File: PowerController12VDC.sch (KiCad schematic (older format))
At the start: 1 part

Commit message: Start power supply
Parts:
- added C?: GRM033R71E331KA01D, CAPC0603X33N, symbol GRM033R71E331KA01D:GRM033R71E331KA01D
- added C?: C3216X6S1V106K160AC, CAPC3216X180N, symbol C3216X6S1V106K160AC:C3216X6S1V106K160AC
- added C?: EEE-FK1E330P, CAPAE660X610N, symbol EEE-FK1E330P:EEE-FK1E330P
- added L?: LQM18PNR47NC0L, INDC1608X55N, symbol LQM18PNR47NC0L:LQM18PNR47NC0L
- added R?: ERJ-3RSFR10V, RESC1608X55N, symbol ERJ-3RSFR10V:ERJ-3RSFR10V
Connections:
- net labels added: +12V, GND
- wire segments 0 -> 18
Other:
- moved on the sheet: U?
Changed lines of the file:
@@
 L TPSM84209RKHT:TPSM84209RKHT U?
 U 1 1 5FCF8D29
-P 2700 2100
-F 0 "U?" H 2700 2566 50  0000 C CNN
-F 1 "TPSM84209RKHT" H 2700 2475 50  0000 C CNN
-F 2 "VREG_TPSM84209RKHT" H 2700 2100 50  0001 L BNN
-F 3 "" H 2700 2100 50  0001 L BNN
-F 4 "TPSM84209RKHT" H 2700 2100 50  0001 L BNN "MP"
-F 5 "Unavailable" H 2700 2100 50  0001 L BNN "AVAILABILITY"
-F 6 "Texas Instruments" H 2700 2100 50  0001 L BNN "MF"
-F 7 "4.5V-28V Input, 1.2V-6.0V Output, 2.5-A Power Module 9-QFN-FCMOD -40 to 85" H 2700 2100 50  0001 L BNN "DESCRIPTION"
-F 8 "PowerQFN-9 Texas Instruments" H 2700 2100 50  0001 L BNN "PACKAGE"
-F 9 "Manufacturer Recommendations" H 2700 2100 50  0001 L BNN "STANDARD"
-F 10 "None" H 2700 2100 50  0001 L BNN "PRICE"
-F 11 "C" H 2700 2100 50  0001 L BNN "PARTREV"
-	1    2700 2100
+P 5450 2050
+F 0 "U?" H 5450 2516 50  0000 C CNN
+F 1 "TPSM84209RKHT" H 5450 2425 50  0000 C CNN
+F 2 "VREG_TPSM84209RKHT" H 5450 2050 50  0001 L BNN
+F 3 "" H 5450 2050 50  0001 L BNN
+F 4 "TPSM84209RKHT" H 5450 2050 50  0001 L BNN "MP"
+F 5 "Unavailable" H 5450 2050 50  0001 L BNN "AVAILABILITY"
+F 6 "Texas Instruments" H 5450 2050 50  0001 L BNN "MF"
+F 7 "4.5V-28V Input, 1.2V-6.0V Output, 2.5-A Power Module 9-QFN-FCMOD -40 to 85" H 5450 2050 50  0001 L BNN "DESCRIPTION"
+F 8 "PowerQFN-9 Texas Instruments" H 5450 2050 50  0001 L BNN "PACKAGE"
+F 9 "Manufacturer Recommendations" H 5450 2050 50  0001 L BNN "STANDARD"
+F 10 "None" H 5450 2050 50  0001 L BNN "PRICE"
+F 11 "C" H 5450 2050 50  0001 L BNN "PARTREV"
+	1    5450 2050
 	1    0    0    -1
 $EndComp
+$Comp
+L GRM033R71E331KA01D:GRM033R71E331KA01D C?
+U 1 1 5FCFC38C
+P 5350 2650
+F 0 "C?" H 5400 2890 50  0000 C CNN
+F 1 "GRM033R71E331KA01D" H 5400 2799 50  0000 C CNN
+F 2 "CAPC0603X33N" H 5350 2650 50  0001 L BNN
+F 3 "" H 5350 2650 50  0001 L BNN
+	1    5350 2650
+	1    0    0    -1
+$EndComp
+Wire Wire Line
+	5550 2650 6350 2650
+Wire Wire Line
+	6350 2650 6350 1850
+Wire Wire Line
+	6350 1850 6150 1850
+Wire Wire Line
+	5250 2650 4500 2650
+Wire Wire Line
+	4500 2650 4500 2050
+Wire Wire Line
+	4500 2050 4750 2050
+$Comp
+L LQM18PNR47NC0L:LQM18PNR47NC0L L?
+U 1 1 5FCFC9A3
+P 1350 1850
+F 0 "L?" H 1350 2031 50  0000 C CNN
+F 1 "LQM18PNR47NC0L" H 1350 1940 50  0000 C CNN
+F 2 "INDC1608X55N" H 1350 1850 50  0001 L BNN
+F 3 "" H 1350 1850 50  0001 L BNN
+	1    1350 1850
+	1    0    0    -1
+$EndComp
+$Comp
+L power:+12V #PWR?
+U 1 1 5FCFF530
+P 700 1850
+F 0 "#PWR?" H 700 1700 50  0001 C CNN
+F 1 "+12V" H 715 2023 50  0000 C CNN
+F 2 "" H 700 1850 50  0001 C CNN
+F 3 "" H 700 1850 50  0001 C CNN
+	1    700  1850
+	1    0    0    -1
+$EndComp
+Wire Wire Line
+	700  1850 1050 1850
+$Comp
+L power:GND #PWR?
+U 1 1 5FCFFBAC
+P 750 3500
+F 0 "#PWR?" H 750 3250 50  0001 C CNN
+F 1 "GND" H 755 3327 50  0000 C CNN
+F 2 "" H 750 3500 50  0001 C CNN
+F 3 "" H 750 3500 50  0001 C CNN
+	1    750  3500
+	1    0    0    -1
+$EndComp
+$Comp
+L C3216X6S1V106K160AC:C3216X6S1V106K160AC C?
+U 1 1 5FD0151A
+P 1050 2850
+F 0 "C?" V 1054 2953 50  0000 L CNN
+F 1 "C3216X6S1V106K160AC" V 1145 2953 50  0000 L CNN
+F 2 "CAPC3216X180N" H 1050 2850 50  0001 L BNN
+F 3 "" H 1050 2850 50  0001 L BNN
+	1    1050 2850
+	0    1    1    0
+$EndComp
+Connection ~ 1050 1850
+$Comp
+L ERJ-3RSFR10V:ERJ-3RSFR10V R?
+U 1 1 5FD02F93
+P 2350 2350
+F 0 "R?" V 2304 2455 50  0000 L CNN
+F 1 "ERJ-3RSFR10V" V 2395 2455 50  0000 L CNN
+F 2 "RESC1608X55N" H 2350 2350 50  0001 L BNN
+F 3 "" H 2350 2350 50  0001 L BNN
+	1    2350 2350
+	0    1    1    0
+$EndComp
+Wire Wire Line
+	1650 1850 2350 1850
+Wire Wire Line
+	2350 1950 2350 1850
+Connection ~ 2350 1850
+Wire Wire Line
+	2350 1850 4750 1850
+Wire Wire Line
+	750  3500 1050 3500
+Wire Wire Line
+	6150 3500 6150 2250
+Wire Wire Line
+	1050 1850 1050 2750
+Wire Wire Line
+	1050 3050 1050 3500
+Connection ~ 1050 3500
+$Comp
+L EEE-FK1E330P:EEE-FK1E330P C?
+U 1 1 5FD07E50
+P 2350 2900
+F 0 "C?" V 2554 3030 50  0000 L CNN
+F 1 "EEE-FK1E330P" V 2645 3030 50  0000 L CNN
+F 2 "CAPAE660X610N" H 2700 2950 50  0001 L CNN
+F 3 "https://industrial.panasonic.com/cdbs/www-data/pdf/RDE0000/ABA0000C1181.pdf" H 2700 2850 50  0001 L CNN
+F 4 "PANASONIC ELECTRONIC COMPONENTS - EEE-FK1E330P - ALUMINUM ELECTROLYTIC CAPACITOR, 33UF, 20%, 25V, SMD, FULL REEL" H 2700 2750 50  0001 L CNN "Description"
+F 5 "6.1" H 2700 2650 50  0001 L CNN "Height"
+F 6 "Panasonic" H 2700 2550 50  0001 L CNN "Manufacturer_Name"
+F 7 "EEE-FK1E330P" H 2700 2450 50  0001 L CNN "Manufacturer_Part_Number"
+F 8 "" H 2700 2350 50  0001 L CNN "Arrow Part Number"
+F 9 "" H 2700 2250 50  0001 L CNN "Arrow Price/Stock"
+F 10 "667-EEE-FK1E330P" H 2700 2150 50  0001 L CNN "Mouser Part Number"
+F 11 "https://www.mouser.com/Search/Refine.aspx?Keyword=667-EEE-FK1E330P" H 2700 2050 50  0001 L CNN "Mouser Price/Stock"
+	1    2350 2900
+	0    1    1    0
+$EndComp
+Wire Wire Line
+	1050 3500 2350 3500
+Wire Wire Line
+	2350 2750 2350 2900
+Wire Wire Line
+	2350 3400 2350 3500
+Connection ~ 2350 3500
+Wire Wire Line
+	2350 3500 6150 3500
 $EndSCHEMATC

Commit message: Schematics for power supply, MCU
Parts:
- removed C?: GRM033R71E331KA01D, CAPC0603X33N, symbol GRM033R71E331KA01D:GRM033R71E331KA01D
- removed C?: C3216X6S1V106K160AC, CAPC3216X180N, symbol C3216X6S1V106K160AC:C3216X6S1V106K160AC
- removed C?: EEE-FK1E330P, CAPAE660X610N, symbol EEE-FK1E330P:EEE-FK1E330P
- removed L?: LQM18PNR47NC0L, INDC1608X55N, symbol LQM18PNR47NC0L:LQM18PNR47NC0L
- removed R?: ERJ-3RSFR10V, RESC1608X55N, symbol ERJ-3RSFR10V:ERJ-3RSFR10V
- removed U?: TPSM84209RKHT, VREG_TPSM84209RKHT, symbol TPSM84209RKHT:TPSM84209RKHT
- added BT?: Battery_Cell, symbol Device:Battery_Cell
- added C?: 10nF, symbol Device:CP1
- added C? (x7): 1uF, symbol Device:CP1
- added C? (x6): 100nF, symbol Device:CP1
- added C?: CP1, symbol Device:CP1
- added C? (x2): 10pF, symbol Device:CP1
- added C? (x2): 2.2uF, symbol Device:C_Small
- added J1: Screw_Terminal_01x02, symbol Connector:Screw_Terminal_01x02
- added J?: Conn_ARM_JTAG_SWD_10, symbol Connector:Conn_ARM_JTAG_SWD_10
- added L?: 22uH, symbol Device:L
- added R? (x4): 10k, symbol Device:R_Small_US
- added R?: R_Small_US, symbol Device:R_Small_US
- added SW?: RESET, symbol Switch:SW_Push
- added U?: STM32F439VITx, Package_QFP:LQFP-100_14x14mm_P0.5mm, symbol MCU_ST_STM32F4:STM32F439VITx
- added Y?: 26MHz, symbol Device:Crystal
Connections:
- net labels added: TCK, TDI, TDO, TMS, VDD
- net labels removed: +12V
- wire segments 18 -> 92

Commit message: Proofread MCU
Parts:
- removed BT?: Battery_Cell, symbol Device:Battery_Cell
- removed C?: CP1, symbol Device:CP1
- added C25: C, symbol Device:C
- added C6: 100nF, symbol Device:C
- C10, C7: renamed from C?; value 10pF -> 4.3pF
- R8: renamed from R?; value R_Small_US -> 100K
- Y1: renamed from Y?; value 26MHz -> NX3225GD-8.000M-EXS00A-CG04874
- gave numbers to parts that had none: 24
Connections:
- net GND: now also C25.2, C6.2
- net VDD: now also J2.1 (VTref), R4.1, R5.1, R6.1, R7.1, U2.6 (VBAT), C25.1
- net NRST: now reaches J2.10 (~RESET~), SW1.2, U2.14 (NRST)
- net NRST: now also C6.1
- net VREF+: now reaches C18.1, C21.1, L2.2, U2.21 (VREF+), U2.22 (VDDA)
- no-connect marks 0 -> 76
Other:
- moved on the sheet: C10, C11, C12, C13, C14, C15, C16, C17, C18, C19, C20, C21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

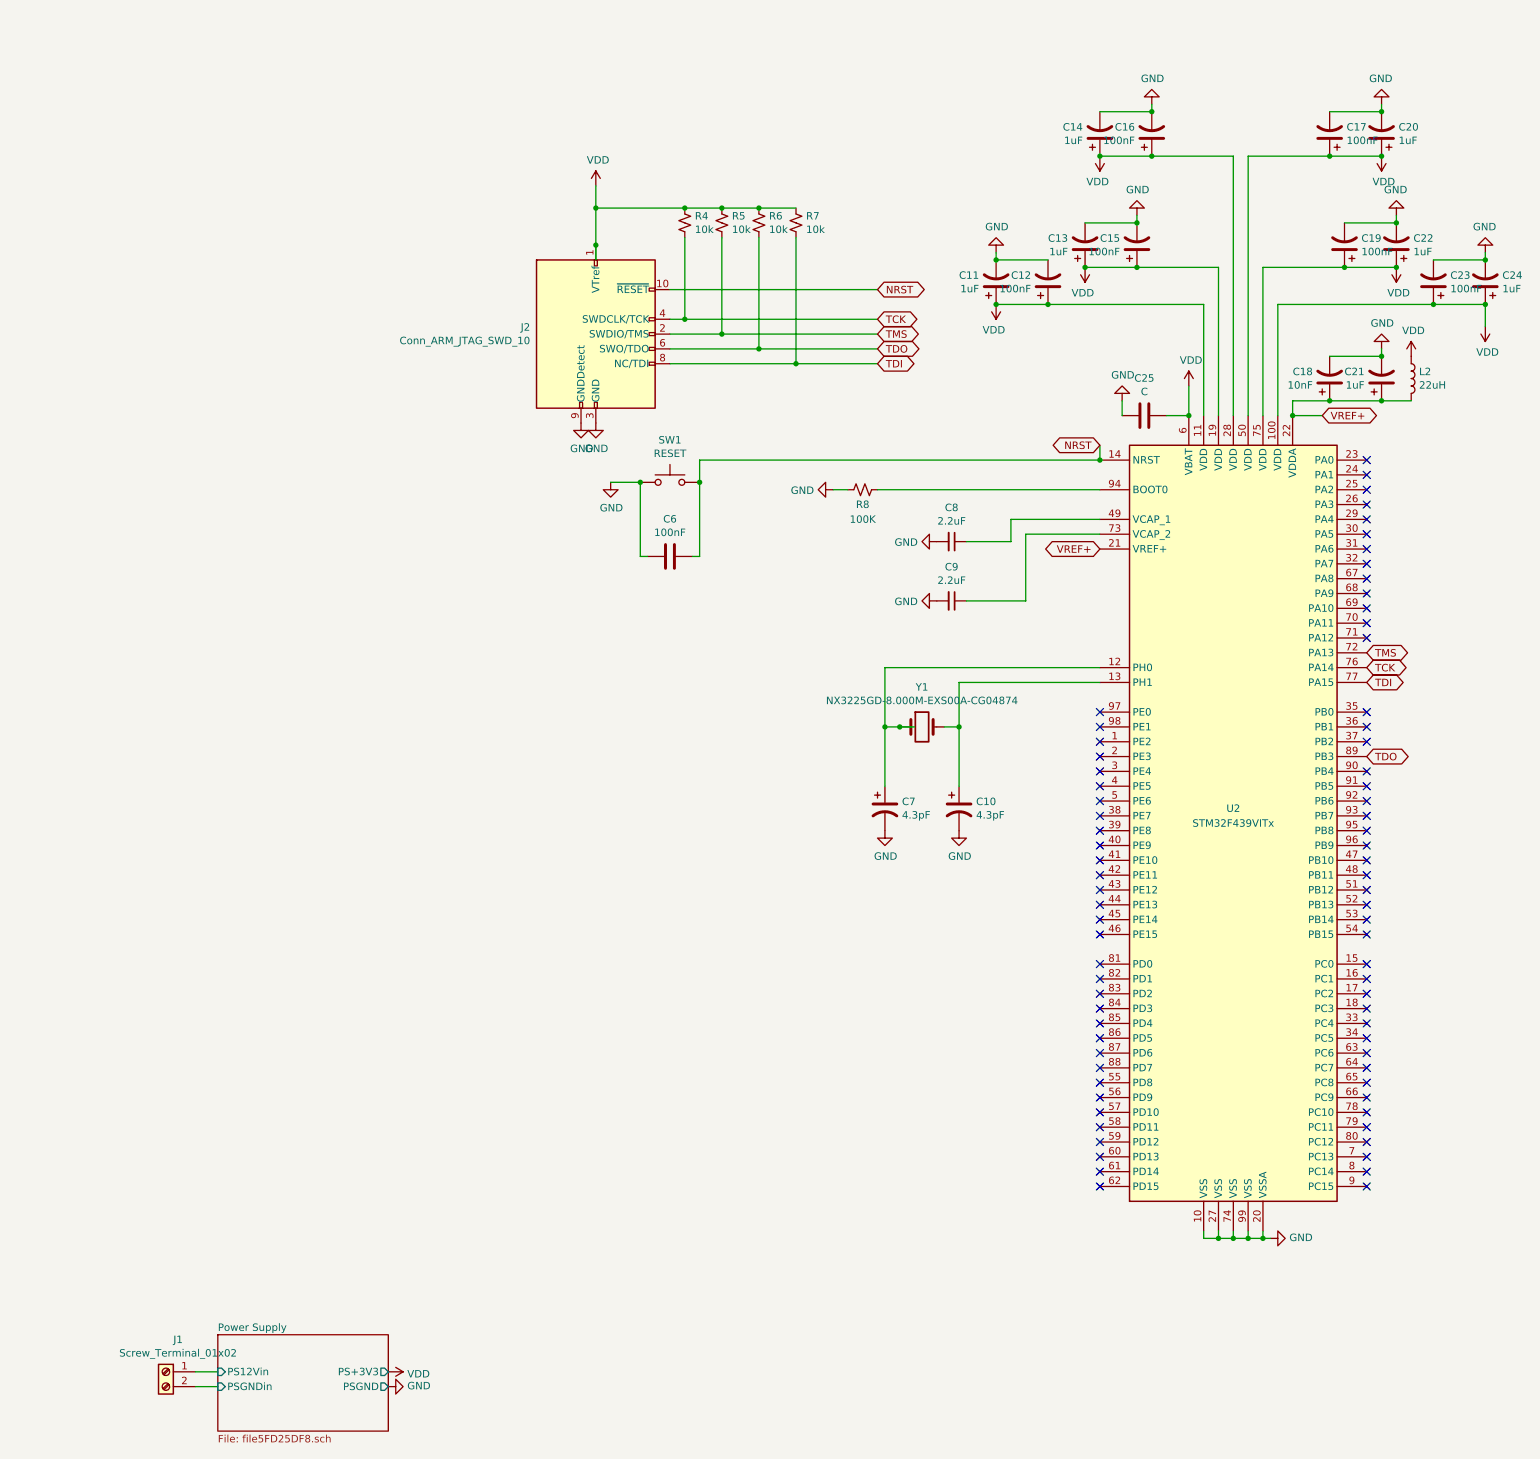
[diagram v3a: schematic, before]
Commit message: Expand hierarchy, reorganize
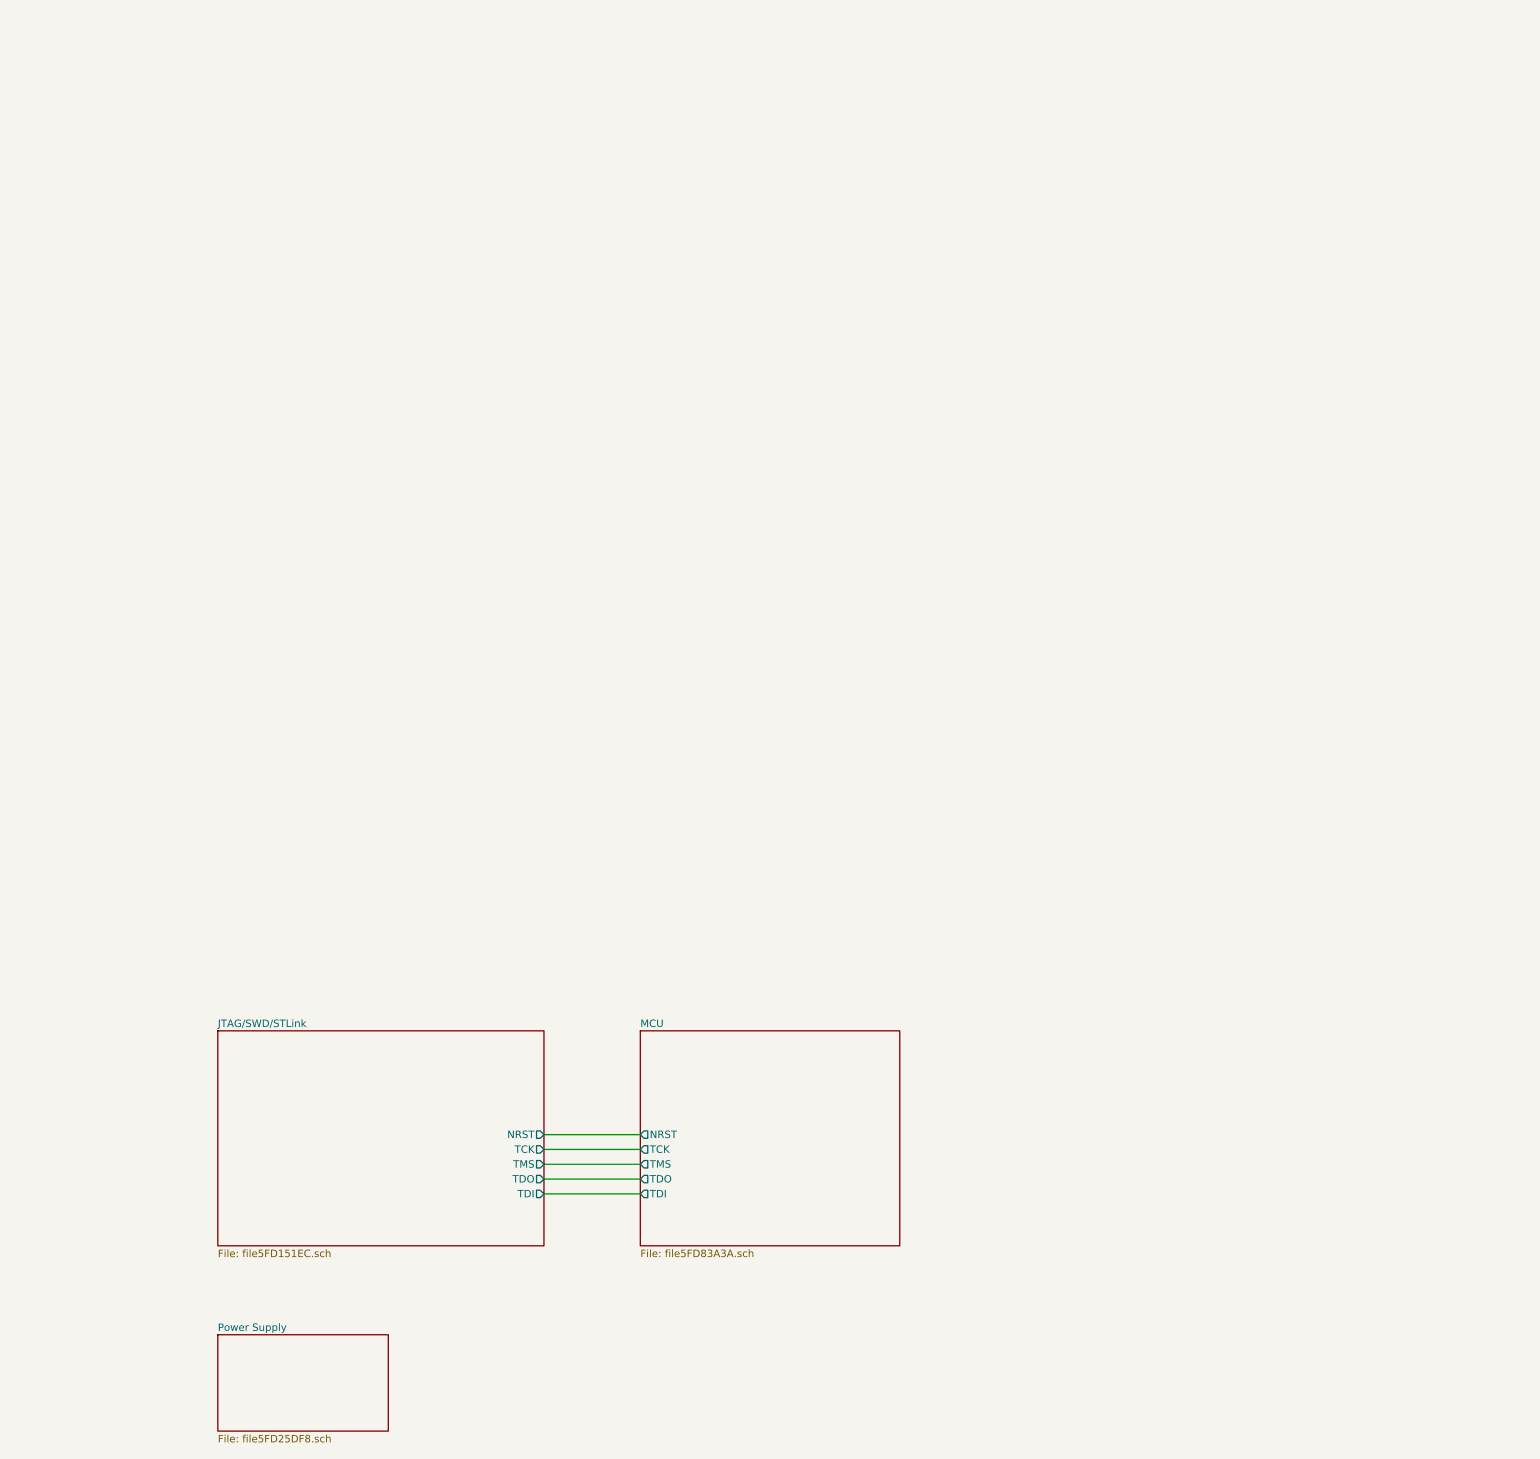
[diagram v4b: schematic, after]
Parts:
- removed C10, C7: 4.3pF, symbol Device:CP1
- removed C11, C13, C14, C20, C21, C22, C24: 1uF, symbol Device:CP1
- removed C12, C15, C16, C17, C19, C23: 100nF, symbol Device:CP1
- removed C18: 10nF, symbol Device:CP1
- removed C25: C, symbol Device:C
- removed C6: 100nF, symbol Device:C
- removed C8, C9: 2.2uF, symbol Device:C_Small
- removed J1: Screw_Terminal_01x02, symbol Connector:Screw_Terminal_01x02
- removed J2: Conn_ARM_JTAG_SWD_10, symbol Connector:Conn_ARM_JTAG_SWD_10
- removed L2: 22uH, symbol Device:L
- removed R4, R5, R6, R7: 10k, symbol Device:R_Small_US
- removed R8: 100K, symbol Device:R_Small_US
- removed SW1: RESET, symbol Switch:SW_Push
- removed U2: STM32F439VITx, Package_QFP:LQFP-100_14x14mm_P0.5mm, symbol MCU_ST_STM32F4:STM32F439VITx
- removed Y1: NX3225GD-8.000M-EXS00A-CG04874, symbol Device:Crystal
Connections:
- no-connect marks 76 -> 0
